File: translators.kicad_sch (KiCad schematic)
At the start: 53 parts, among them U12 SN74AXC8T245RJWR, U3 SN74AXC8T245RJWR, U6 SN74AXC8T245RJWR

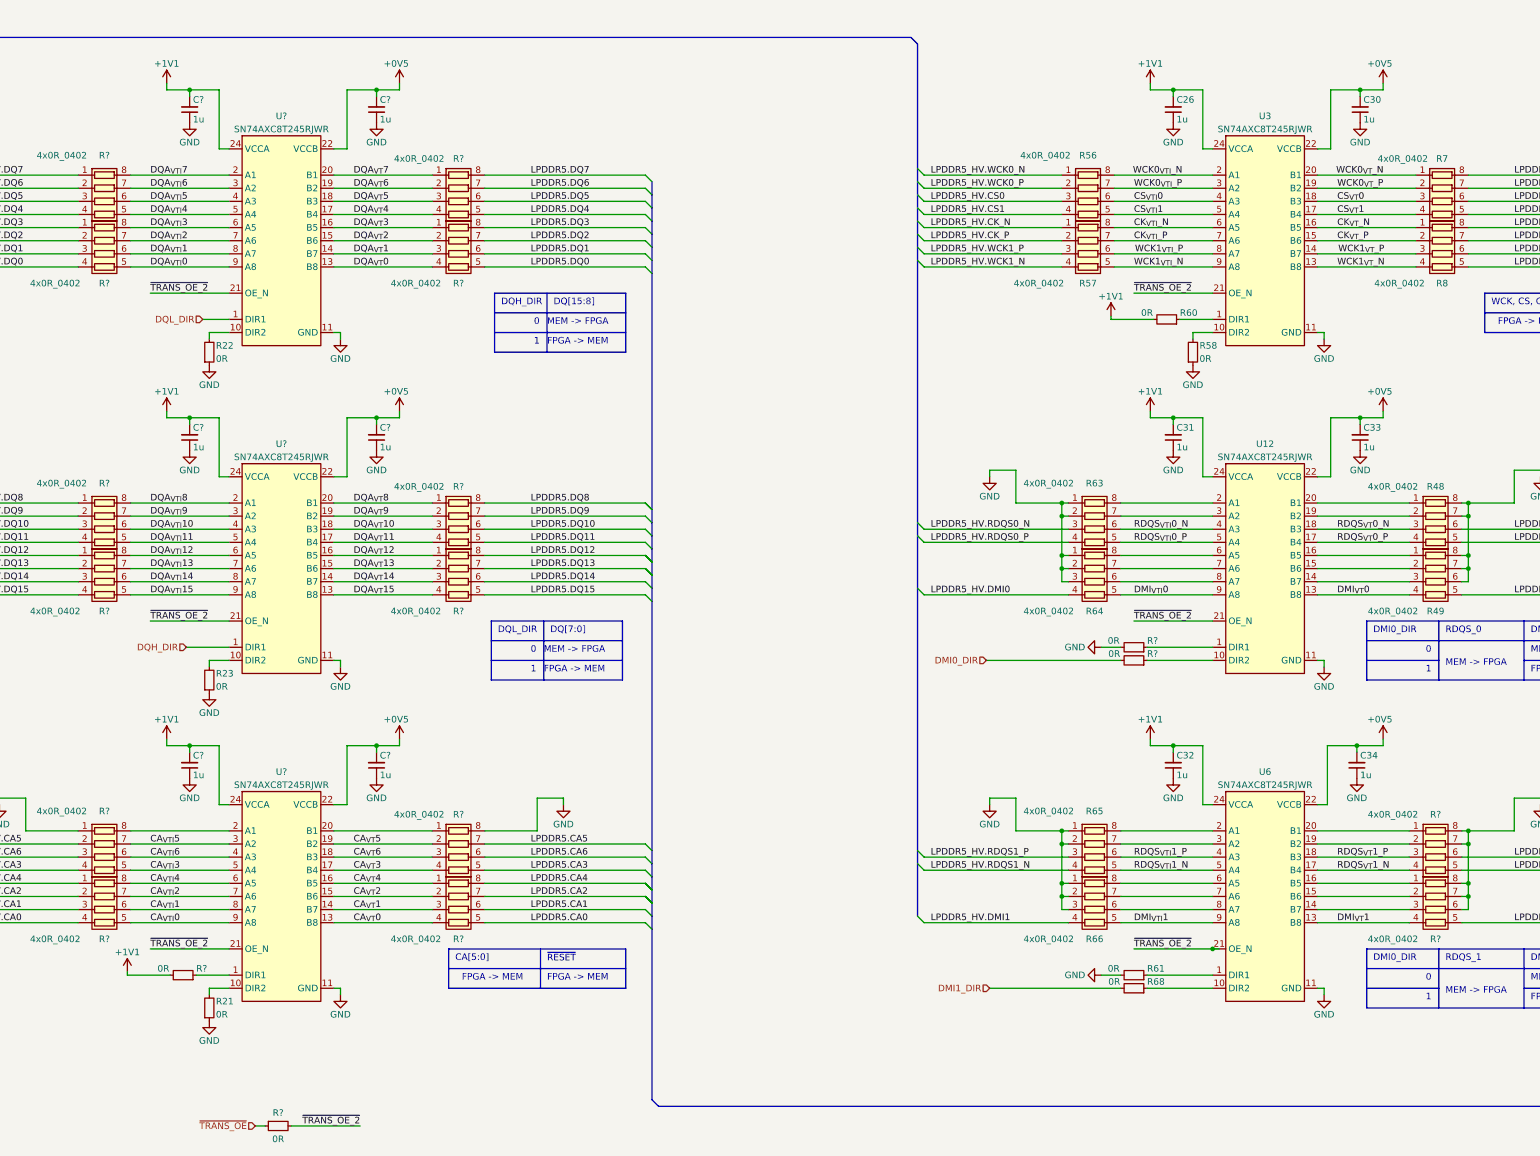
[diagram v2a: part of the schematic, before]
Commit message: [#52835] schematics: update components after standardization
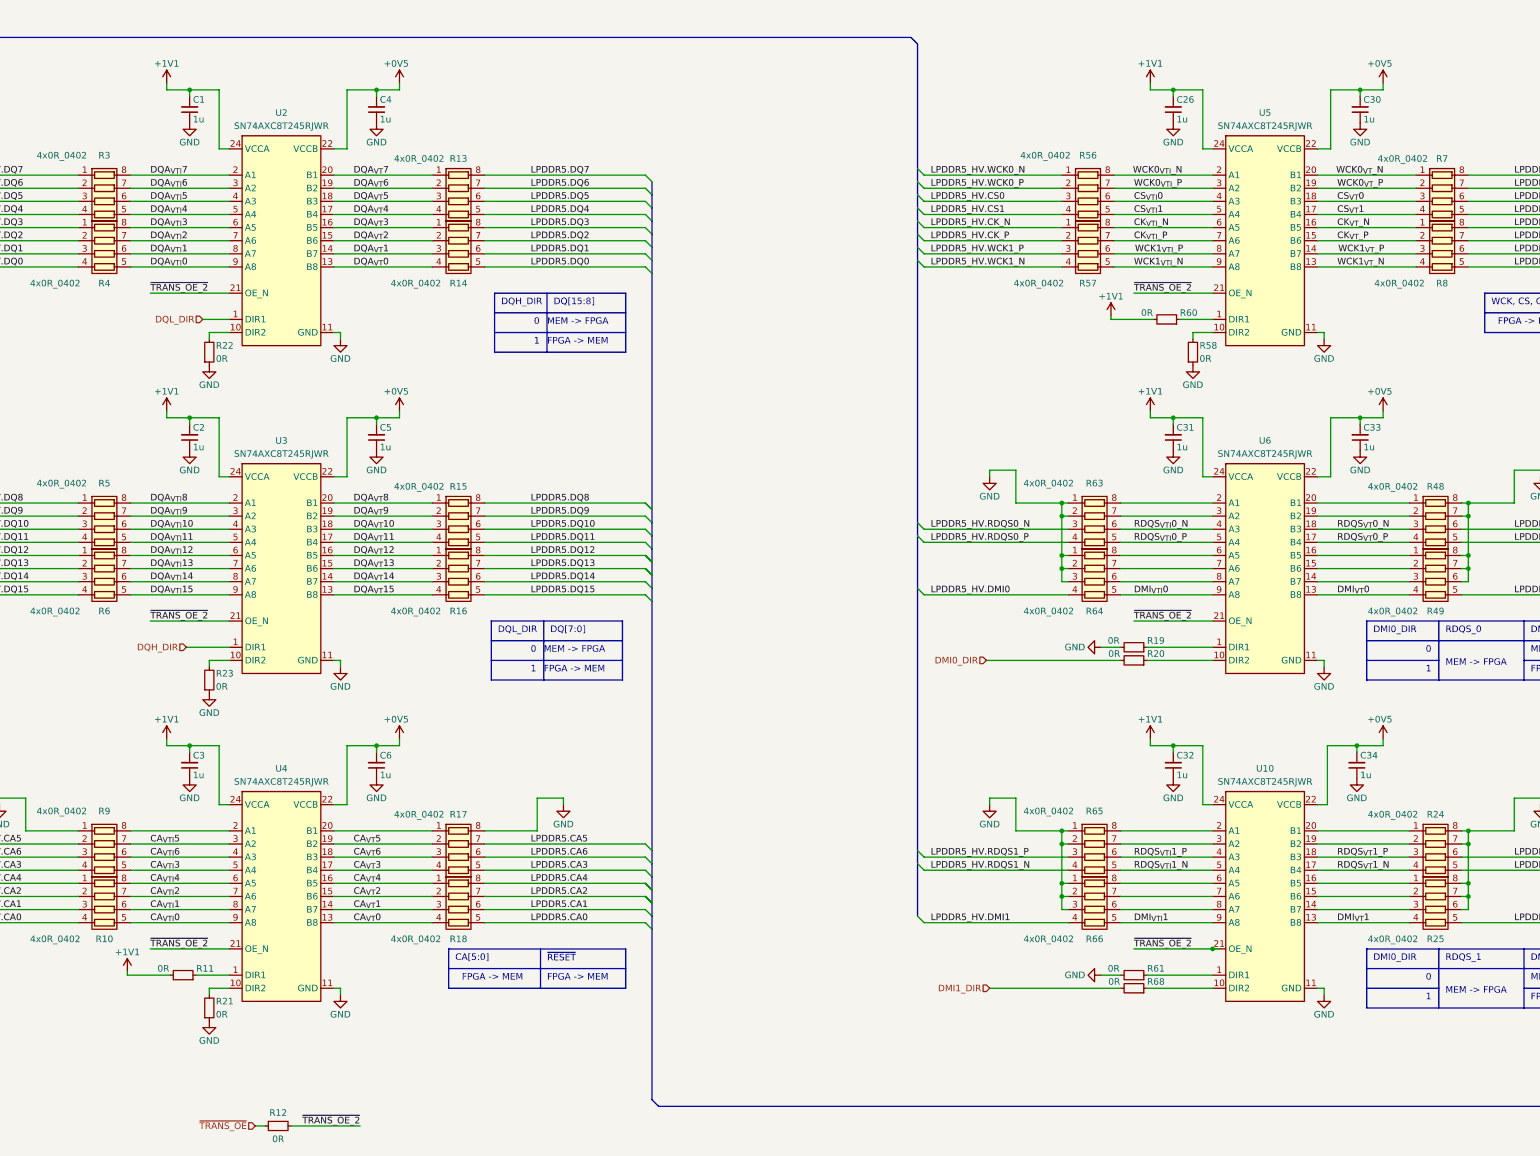
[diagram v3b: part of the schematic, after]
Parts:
- removed U12, U3, U6, U? (x3): SN74AXC8T245RJWR, antmicro-footprints:UQFN-28-2x4mm_P0.4mm_Texas_RJW0024A, symbol antmicroLogicTranslatorsLevelShifters:SN74AXC8T245RJWR
- added U10, U2, U3, U4, U5, U6: SN74AXC8T245_UQFN, antmicro-footprints:UQFN-24_2x4mm_P0.4mm_Texas_RJW0024A, symbol antmicroLogicTranslatorsLevelShifters:SN74AXC8T245_UQFN
- gave numbers to parts that had none: 24
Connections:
- net +0V5: now also U10.22 (VCCB), U10.23 (VCCB), U2.22 (VCCB), U2.23 (VCCB), U3.22 (VCCB), U3.23 (VCCB), U4.22 (VCCB), U4.23 (VCCB), U5.22 (VCCB), U5.23 (VCCB), U6.22 (VCCB), U6.23 (VCCB)
- net +1V1: now also U10.24 (VCCA), U2.24 (VCCA), U3.24 (VCCA), U4.24 (VCCA), U5.24 (VCCA), U6.24 (VCCA)
- net CA_{VTI}0: now also U4.9 (A8)
- net CA_{VTI}1: now also U4.8 (A7)
- net CA_{VTI}2: now also U4.7 (A6)
- net CA_{VTI}3: now also U4.5 (A4)
- net CA_{VTI}4: now also U4.6 (A5)
- net CA_{VTI}5: now also U4.3 (A2)
- net CA_{VTI}6: now also U4.4 (A3)
- net CA_{VT}0: now also U4.13 (B8)
- net CA_{VT}1: now also U4.14 (B7)
- net CA_{VT}2: now also U4.15 (B6)
- net CA_{VT}3: now also U4.17 (B4)
- net CA_{VT}4: now also U4.16 (B5)
- net CA_{VT}5: now also U4.19 (B2)
- net CA_{VT}6: now also U4.18 (B3)
- net CK_{VTI}_N: now also U5.6 (A5)
- net CK_{VTI}_P: now also U5.7 (A6)
- net CK_{VT}_N: now also U5.16 (B5)
- net CK_{VT}_P: now also U5.15 (B6)
- net CS_{VTI}0: now also U5.4 (A3)
- net CS_{VTI}1: now also U5.5 (A4)
- net CS_{VT}0: now also U5.18 (B3)
- net CS_{VT}1: now also U5.17 (B4)
- net DMI_{VTI}0: now also U6.9 (A8)
- net DMI_{VTI}1: now also U10.9 (A8)
- net DMI_{VT}0: now also U6.13 (B8)
- net DMI_{VT}1: now also U10.13 (B8)
- net DQA_{VTI}0: now also U2.9 (A8)
- net DQA_{VTI}1: now also U2.8 (A7)
- net DQA_{VTI}10: now also U3.4 (A3)
- net DQA_{VTI}11: now also U3.5 (A4)
- net DQA_{VTI}12: now also U3.6 (A5)
- net DQA_{VTI}13: now also U3.7 (A6)
- net DQA_{VTI}14: now also U3.8 (A7)
- net DQA_{VTI}15: now also U3.9 (A8)
- net DQA_{VTI}2: now also U2.7 (A6)
- net DQA_{VTI}3: now also U2.6 (A5)
- net DQA_{VTI}4: now also U2.5 (A4)
- net DQA_{VTI}5: now also U2.4 (A3)
- net DQA_{VTI}6: now also U2.3 (A2)
- net DQA_{VTI}7: now also U2.2 (A1)
- net DQA_{VTI}8: now also U3.2 (A1)
- net DQA_{VTI}9: now also U3.3 (A2)
- net DQA_{VT}0: now also U2.13 (B8)
- net DQA_{VT}1: now also U2.14 (B7)
- net DQA_{VT}10: now also U3.18 (B3)
- net DQA_{VT}11: now also U3.17 (B4)
- net DQA_{VT}12: now also U3.16 (B5)
- net DQA_{VT}13: now also U3.15 (B6)
- net DQA_{VT}14: now also U3.14 (B7)
- net DQA_{VT}15: now also U3.13 (B8)
- net DQA_{VT}2: now also U2.15 (B6)
- net DQA_{VT}3: now also U2.16 (B5)
- net DQA_{VT}4: now also U2.17 (B4)
- net DQA_{VT}5: now also U2.18 (B3)
- net DQA_{VT}6: now also U2.19 (B2)
- net DQA_{VT}7: now also U2.20 (B1)
- net DQA_{VT}8: now also U3.20 (B1)
- net DQA_{VT}9: now also U3.19 (B2)
- net DQH_DIR: now also U3.1 (DIR1)
- net DQL_DIR: now also U2.1 (DIR1)
- net GND: now also U10.11 (GND), U10.12 (GND), U2.11 (GND), U2.12 (GND), U3.11 (GND), U3.12 (GND), U4.11 (GND), U4.12 (GND), U5.11 (GND), U5.12 (GND), U6.11 (GND), U6.12 (GND)
- net RDQS_{VTI}0_N: now also U6.4 (A3)
- net RDQS_{VTI}0_P: now also U6.5 (A4)
- net RDQS_{VTI}1_N: now also U10.5 (A4)
- net RDQS_{VTI}1_P: now also U10.4 (A3)
- net RDQS_{VT}0_N: now also U6.18 (B3)
- net RDQS_{VT}0_P: now also U6.17 (B4)
- net RDQS_{VT}1_N: now also U10.17 (B4)
- net RDQS_{VT}1_P: now also U10.18 (B3)
- net WCK0_{VTI}_N: now also U5.2 (A1)
- net WCK0_{VTI}_P: now also U5.3 (A2)
- net WCK0_{VT}_N: now also U5.20 (B1)
- net WCK0_{VT}_P: now also U5.19 (B2)
- net WCK1_{VTI}_N: now also U5.9 (A8)
- net WCK1_{VTI}_P: now also U5.8 (A7)
- net WCK1_{VT}_N: now also U5.13 (B8)
- net WCK1_{VT}_P: now also U5.14 (B7)
- net ~{TRANS_OE_2}: now also U10.21 (OE_N), U2.21 (OE_N), U3.21 (OE_N), U4.21 (OE_N), U5.21 (OE_N), U6.21 (OE_N)
- net at R49.1 (R1.1): now also U6.16 (B5)
- net at R49.2 (R2.1): now also U6.15 (B6)
- net at R49.3 (R3.1): now also U6.14 (B7)
- net at R25.1 (R1.1): now also U10.16 (B5)
- net at R25.2 (R2.1): now also U10.15 (B6)
- net at R25.3 (R3.1): now also U10.14 (B7)
- net at R23.2: now also U3.10 (DIR2)
- net at R60.1: now also U5.1 (DIR1)
- net at R19.1: now also U6.1 (DIR1)
- net at R20.1: now also U6.10 (DIR2)
- net at R48.2 (R2.1): now also U6.19 (B2)
- net at R63.8 (R1.2): now also U6.2 (A1)
- net at R48.1 (R1.1): now also U6.20 (B1)
- net at R63.7 (R2.2): now also U6.3 (A2)
- net at R64.8 (R1.2): now also U6.6 (A5)
- net at R64.7 (R2.2): now also U6.7 (A6)
- net at R64.6 (R3.2): now also U6.8 (A7)
- net at R22.2: now also U2.10 (DIR2)
- net at R58.2: now also U5.10 (DIR2)
- net at R68.1: now also U10.10 (DIR2)
- net at R65.7 (R2.2): now also U10.3 (A2)
- net at R65.8 (R1.2): now also U10.2 (A1)
- net at R17.1 (R1.1): now also U4.20 (B1)
- net at R66.6 (R3.2): now also U10.8 (A7)
- net at R66.7 (R2.2): now also U10.7 (A6)
- net at R66.8 (R1.2): now also U10.6 (A5)
- net at R61.1: now also U10.1 (DIR1)
- net at R11.1: now also U4.1 (DIR1)
- net at R21.2: now also U4.10 (DIR2)
- net at R9.8 (R1.2): now also U4.2 (A1)
- net at R24.2 (R2.1): now also U10.19 (B2)
- net at R24.1 (R1.1): now also U10.20 (B1)
